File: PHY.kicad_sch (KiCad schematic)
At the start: 50 parts, among them U1 LAN83C185-JT, Y1 25 MHz

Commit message: Assign footprints to everything bar inductors
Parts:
- C5, C7: footprint (none) -> Capacitor_SMD:C_0805_2012Metric_Pad1.18x1.45mm_HandSolder
- D1, D2: footprint (none) -> LED_SMD:LED_1206_3216Metric_Pad1.42x1.75mm_HandSolder
- FB1, FB2, FB3: footprint (none) -> Inductor_SMD:L_1206_3216Metric_Pad1.22x1.90mm_HandSolder
- JP1, JP2, JP3, JP4: footprint (none) -> Jumper:SolderJumper-2_P1.3mm_Open_Pad1.0x1.5mm
- TP1: footprint (none) -> TestPoint:TestPoint_Pad_1.0x1.0mm
- Y1: footprint (none) -> Crystal:Crystal_SMD_Abracon_ABM3-2Pin_5.0x3.2mm_HandSoldering
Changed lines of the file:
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@@
       (effects (font (size 1.27 1.27)) (justify left))
     )
-    (property "Footprint" "" (id 2) (at 231.14 100.33 0)
+    (property "Footprint" "TestPoint:TestPoint_Pad_1.0x1.0mm" (id 2) (at 231.14 100.33 0)
       (effects (font (size 1.27 1.27)) hide)
     )
@@
     (property "Reference" "FB3" (id 0) (at 115.5192 165.1 90))
     (property "Value" "FerriteBead" (id 1) (at 115.5192 167.64 90))
-    (property "Footprint" "" (id 2) (at 115.57 174.498 90)
+    (property "Footprint" "Inductor_SMD:L_1206_3216Metric_Pad1.22x1.90mm_HandSolder" (id 2) (at 115.57 174.498 90)
       (effects (font (size 1.27 1.27)) hide)
     )
@@
       (effects (font (size 1.27 1.27)) (justify left))
     )
-    (property "Footprint" "" (id 2) (at 33.9852 129.54 0)
+    (property "Footprint" "Capacitor_SMD:C_0805_2012Metric_Pad1.18x1.45mm_HandSolder" (id 2) (at 33.9852 129.54 0)
       (effects (font (size 1.27 1.27)) hide)
     )
@@
     (property "Reference" "JP4" (id 0) (at 71.12 55.88 0))
     (property "Value" "SolderJumper_2_Open" (id 1) (at 71.12 58.42 0))
-    (property "Footprint" "" (id 2) (at 71.12 62.23 0)
+    (property "Footprint" "Jumper:SolderJumper-2_P1.3mm_Open_Pad1.0x1.5mm" (id 2) (at 71.12 62.23 0)
       (effects (font (size 1.27 1.27)) hide)
     )
@@
     (property "Reference" "JP2" (id 0) (at 71.12 50.8 0))
     (property "Value" "SolderJumper_2_Open" (id 1) (at 71.12 53.34 0))
-    (property "Footprint" "" (id 2) (at 71.12 57.15 0)
+    (property "Footprint" "Jumper:SolderJumper-2_P1.3mm_Open_Pad1.0x1.5mm" (id 2) (at 71.12 57.15 0)
       (effects (font (size 1.27 1.27)) hide)
     )
@@
     (property "Reference" "JP3" (id 0) (at 71.12 53.34 0))
     (property "Value" "SolderJumper_2_Open" (id 1) (at 71.12 55.88 0))
-    (property "Footprint" "" (id 2) (at 71.12 59.69 0)
+    (property "Footprint" "Jumper:SolderJumper-2_P1.3mm_Open_Pad1.0x1.5mm" (id 2) (at 71.12 59.69 0)
       (effects (font (size 1.27 1.27)) hide)
     )
@@
     (property "Reference" "FB1" (id 0) (at 27.8892 165.1 90))
     (property "Value" "FerriteBead" (id 1) (at 27.8892 167.64 90))
-    (property "Footprint" "" (id 2) (at 27.94 174.498 90)
+    (property "Footprint" "Inductor_SMD:L_1206_3216Metric_Pad1.22x1.90mm_HandSolder" (id 2) (at 27.94 174.498 90)
       (effects (font (size 1.27 1.27)) hide)
     )
@@
       (effects (font (size 1.27 1.27)) (justify right))
     )
-    (property "Footprint" "" (id 2) (at 269.24 33.02 0)
+    (property "Footprint" "LED_SMD:LED_1206_3216Metric_Pad1.42x1.75mm_HandSolder" (id 2) (at 269.24 33.02 0)
       (effects (font (size 1.27 1.27)) hide)
     )
@@
     (property "Reference" "FB2" (id 0) (at 79.9592 165.1 90))
     (property "Value" "FerriteBead" (id 1) (at 79.9592 167.64 90))
-    (property "Footprint" "" (id 2) (at 80.01 174.498 90)
+    (property "Footprint" "Inductor_SMD:L_1206_3216Metric_Pad1.22x1.90mm_HandSolder" (id 2) (at 80.01 174.498 90)
       (effects (font (size 1.27 1.27)) hide)
     )
@@
     (property "Reference" "Y1" (id 0) (at 27.94 111.76 0))
     (property "Value" "25 MHz" (id 1) (at 27.94 114.3 0))
-    (property "Footprint" "" (id 2) (at 27.94 119.38 0)
+    (property "Footprint" "Crystal:Crystal_SMD_Abracon_ABM3-2Pin_5.0x3.2mm_HandSoldering" (id 2) (at 27.94 119.38 0)
       (effects (font (size 1.27 1.27)) hide)
     )
@@
     (property "Reference" "JP1" (id 0) (at 71.12 45.72 0))
     (property "Value" "SolderJumper_2_Open" (id 1) (at 71.12 48.26 0))
-    (property "Footprint" "" (id 2) (at 71.12 52.07 0)
+    (property "Footprint" "Jumper:SolderJumper-2_P1.3mm_Open_Pad1.0x1.5mm" (id 2) (at 71.12 52.07 0)
       (effects (font (size 1.27 1.27)) hide)
     )
@@
       (effects (font (size 1.27 1.27)) (justify right))
     )
-    (property "Footprint" "" (id 2) (at 219.71 31.75 0)
+    (property "Footprint" "LED_SMD:LED_1206_3216Metric_Pad1.42x1.75mm_HandSolder" (id 2) (at 219.71 31.75 0)
       (effects (font (size 1.27 1.27)) hide)
     )
@@
       (effects (font (size 1.27 1.27)) (justify left))
     )
-    (property "Footprint" "" (id 2) (at 23.8252 129.54 0)
-      (effects (font (size 1.27 1.27)) hide)
-    )
+    (property "Footprint" "Capacitor_SMD:C_0805_2012Metric_Pad1.18x1.45mm_HandSolder" (id 2) (at 23.8252 129.54 0)
+      (effects (font (size 1.27 1.27)) hide)
+    )

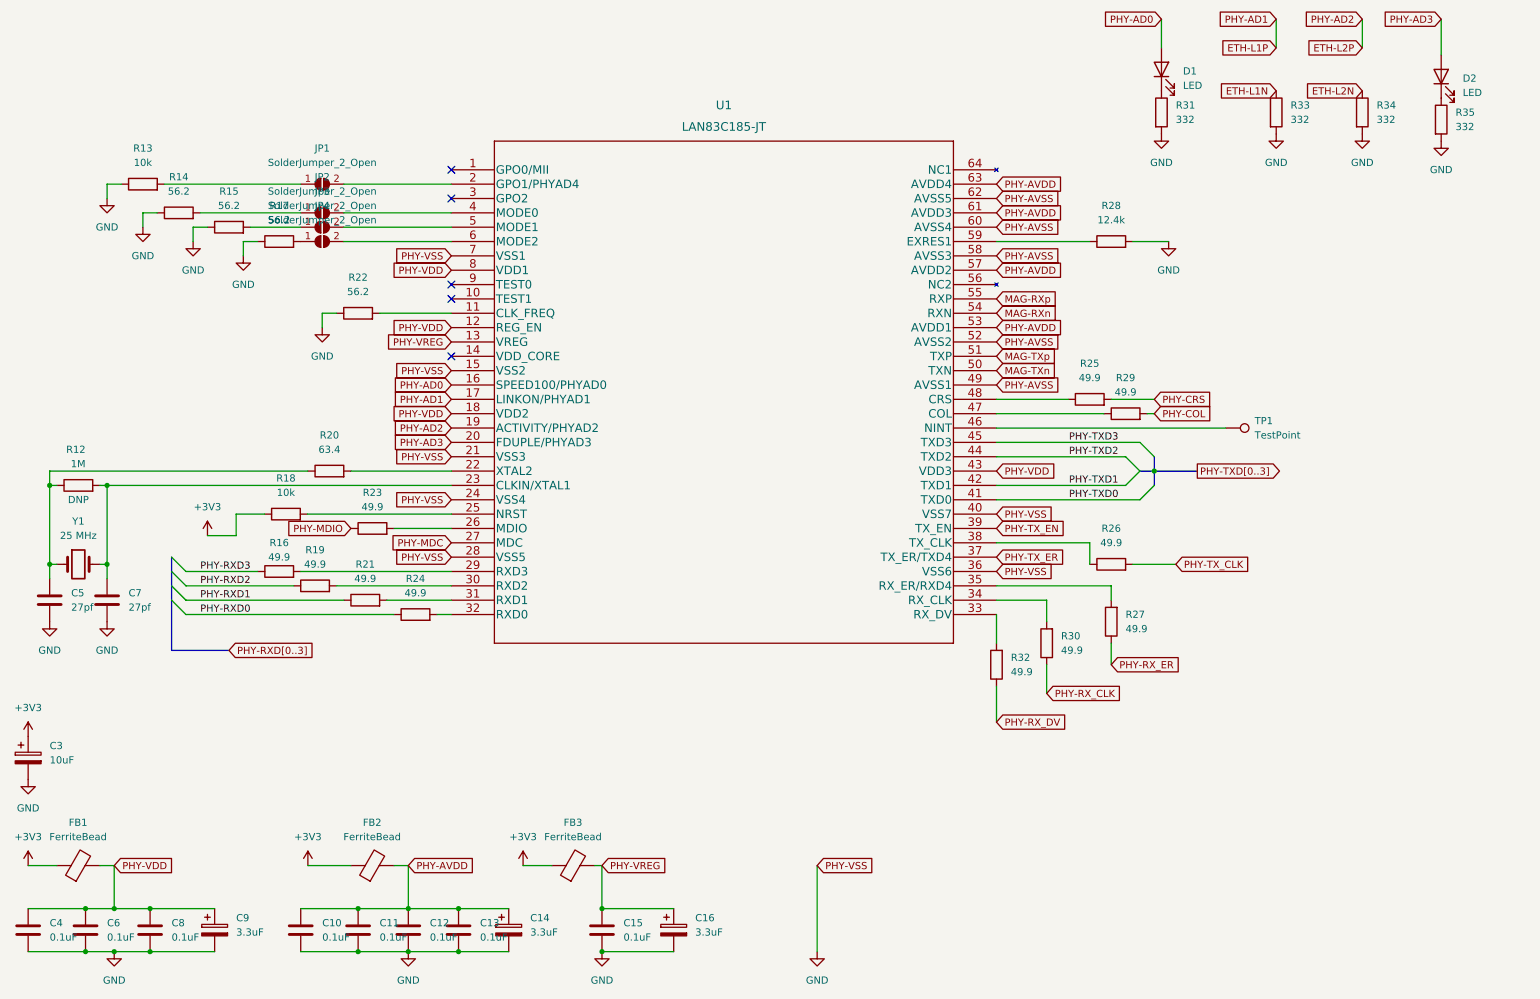
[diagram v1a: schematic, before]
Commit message: added most of the sourcing info
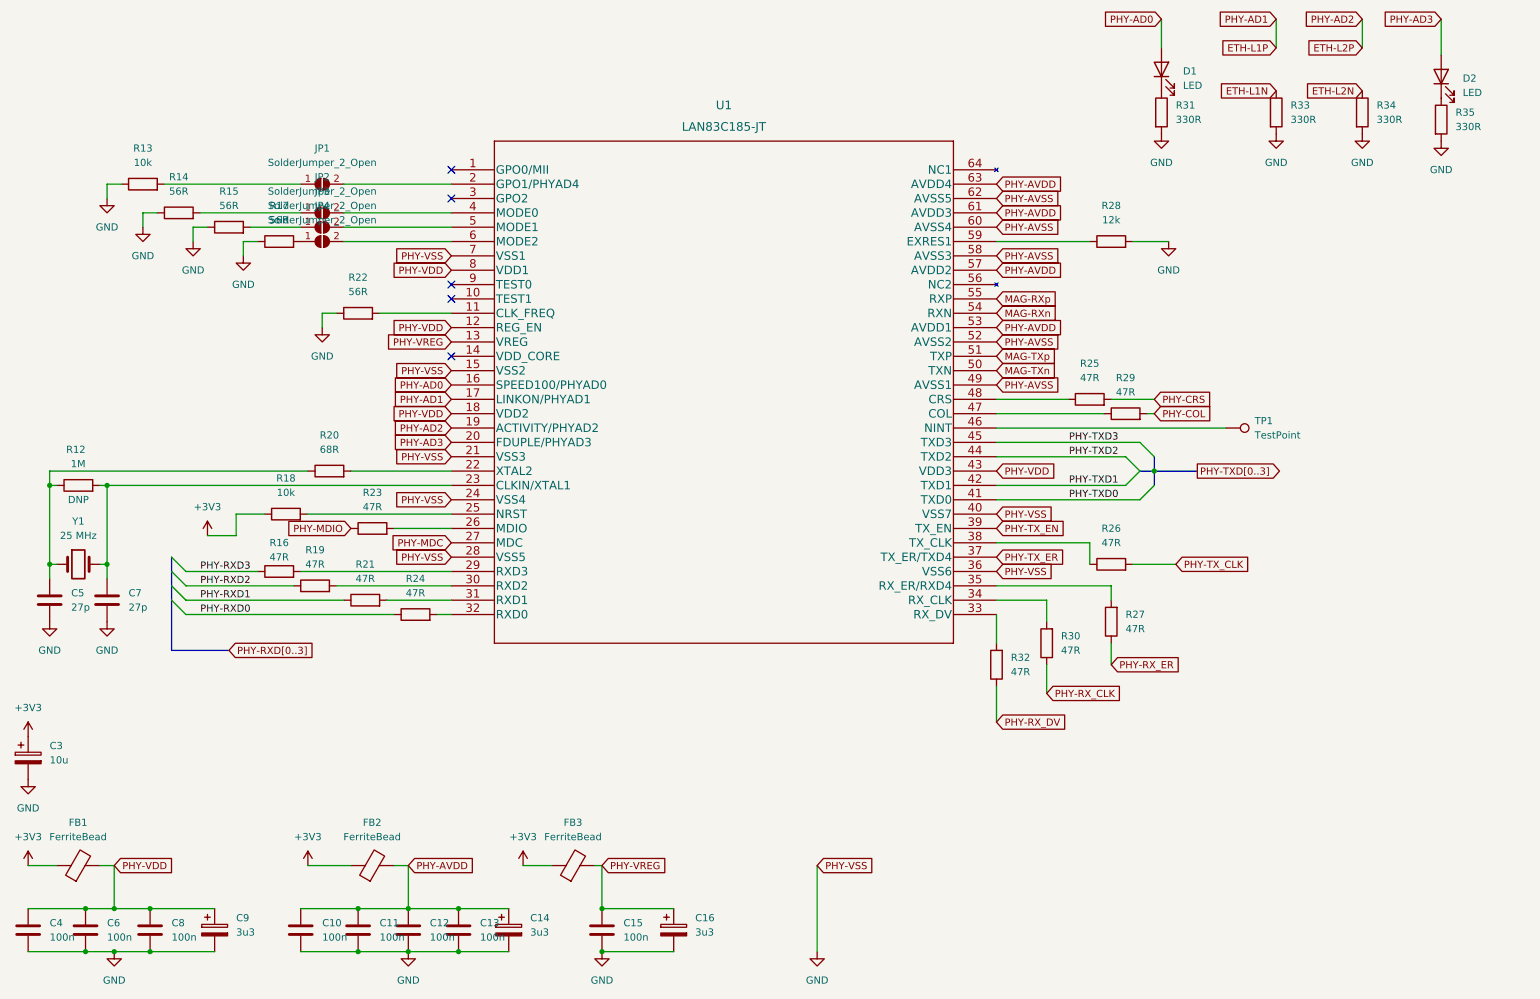
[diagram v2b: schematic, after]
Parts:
- C10, C11, C12, C13, C15, C4, C6, C8: value 0.1uF -> 100n; Source (none) -> L3 store
- C14, C16, C9: value 3.3uF -> 3u3; Source (none) -> L3 store
- C3: value 10uF -> 10u; Source (none) -> L3 store
- C5, C7: value 27pf -> 27p; Source (none) -> https://onecall.farnell.com/multicomp/mc0805n270j500ct/cap-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
- D1: Source (none) -> https://onecall.farnell.com/dialight/599-0240-007f/led-yell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
- D2: Source (none) -> https://onecall.farnell.com/dialight/599-0281-007f/led-gree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
- FB1, FB2, FB3: Source (none) -> https://uk.farnell.com/bourns/mh3261-601y/ferrite-bead-0-1o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
- JP1, JP2, JP3, JP4, TP1: Source (none) -> pcb
- R12, R13, R18: Source (none) -> L3 store
- R14, R15, R17, R22: value 56.2 -> 56R; Source (none) -> L3 store
- R16, R19, R21, R23, R24, R25, R26, R27, R29, R30, R32: value 49.9 -> 47R; Source (none) -> L3 store
- R20: value 63.4 -> 68R; Source (none) -> L3 store
- R28: value 12.4k -> 12k; Source (none) -> L3 store
- R31, R33, R34, R35: value 332 -> 330R; Source (none) -> L3 store
- U1: Source (none) -> https://uk.rs-online.com/web/p/physical-layer-transceivers/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
- Y1: Source (none) -> https://onecall.farnell.com/abracon/abm3-25-000mhz-d2y-t/cr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

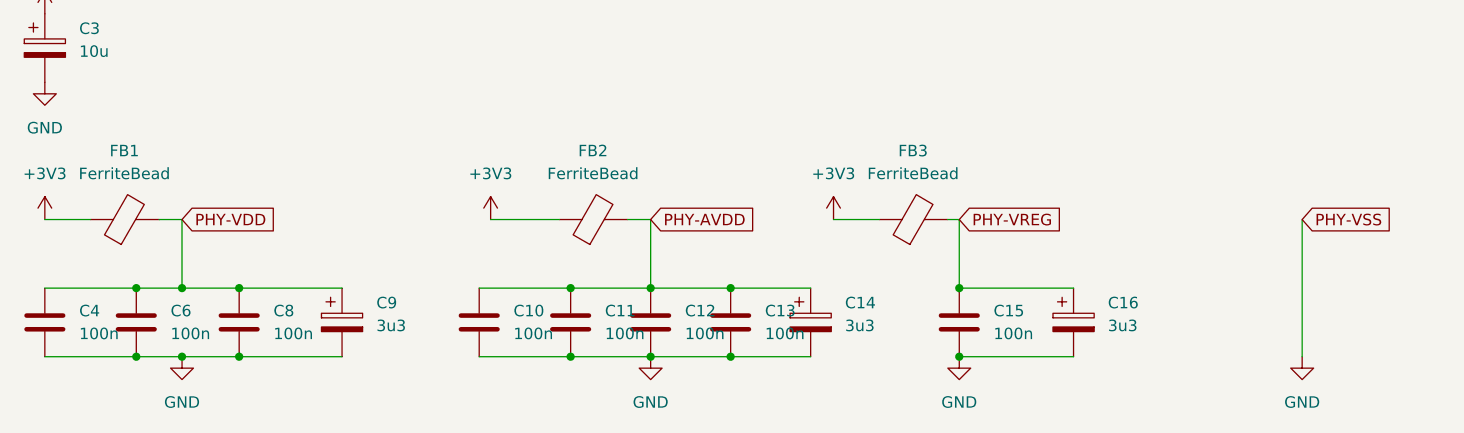
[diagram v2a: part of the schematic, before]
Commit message: solved power drc problems
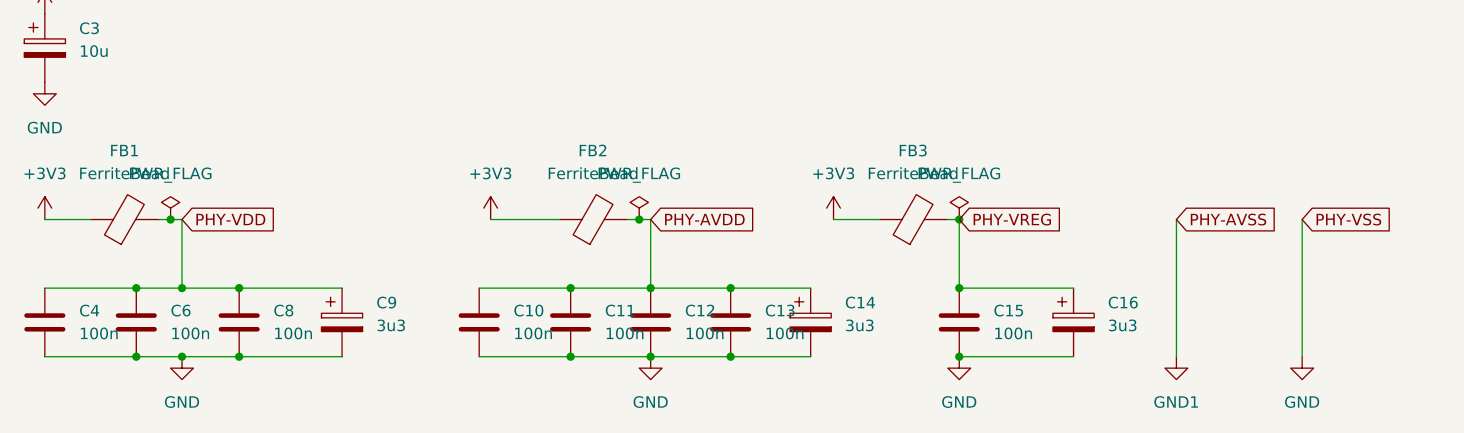
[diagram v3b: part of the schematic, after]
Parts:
- U1: Source https://uk.rs-online.com/web/p/physical-layer-transceivers/9101828 -> https://uk.rs-online.com/web/p/physical-layer-transceivers/6726806
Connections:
- net PHY-AVSS renamed GND1
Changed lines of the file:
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@@
   (junction (at 120.65 187.96) (diameter 0) (color 0 0 0 0)
   )
+  (junction (at 85.09 172.72) (diameter 0) (color 0 0 0 0)
+  )
+  (junction (at 120.65 172.72) (diameter 0) (color 0 0 0 0)
+  )
   (junction (at 34.29 180.34) (diameter 0) (color 0 0 0 0)
   )
@@
   )
   (junction (at 33.02 119.38) (diameter 0) (color 0 0 0 0)
+  )
+  (junction (at 33.02 172.72) (diameter 0) (color 0 0 0 0)
   )
   (junction (at 29.21 180.34) (diameter 0) (color 0 0 0 0)
@@
     (stroke (width 0) (type default) (color 0 0 0 0))
   )
+  (wire (pts (xy 144.78 172.72) (xy 144.78 187.96))
+    (stroke (width 0) (type default) (color 0 0 0 0))
+  )
   (wire (pts (xy 71.12 74.93) (xy 71.12 77.47))
     (stroke (width 0) (type default) (color 0 0 0 0))
@@
     (stroke (width 0) (type default) (color 0 0 0 0))
   )
-  (wire (pts (xy 31.75 172.72) (xy 34.29 172.72))
+  (wire (pts (xy 31.75 172.72) (xy 33.02 172.72))
     (stroke (width 0) (type default) (color 0 0 0 0))
   )
@@
     (stroke (width 0) (type default) (color 0 0 0 0))
   )
+  (wire (pts (xy 85.09 172.72) (xy 86.36 172.72))
+    (stroke (width 0) (type default) (color 0 0 0 0))
+  )
   (wire (pts (xy 255.27 22.86) (xy 255.27 27.94))
     (stroke (width 0) (type default) (color 0 0 0 0))
@@
     (stroke (width 0) (type default) (color 0 0 0 0))
   )
+  (wire (pts (xy 33.02 172.72) (xy 34.29 172.72))
+    (stroke (width 0) (type default) (color 0 0 0 0))
+  )
   (wire (pts (xy 46.99 128.27) (xy 83.82 128.27))
     (stroke (width 0) (type default) (color 0 0 0 0))
@@
     (stroke (width 0) (type default) (color 0 0 0 0))
   )
-  (wire (pts (xy 83.82 172.72) (xy 86.36 172.72))
+  (wire (pts (xy 83.82 172.72) (xy 85.09 172.72))
     (stroke (width 0) (type default) (color 0 0 0 0))
   )
@@
     )
   )
+  (global_label "PHY-AVSS" (shape input) (at 144.78 172.72 0) (fields_autoplaced)
+    (effects (font (size 1.27 1.27)) (justify left))
+    (property "Intersheet References" "${INTERSHEET_REFS}" (id 0) (at 157.0507 172.6406 0)
+      (effects (font (size 1.27 1.27)) (justify left) hide)
+    )
+  )
   (global_label "PHY-AVDD" (shape input) (at 190.5 67.31 0) (fields_autoplaced)
     (effects (font (size 1.27 1.27)) (justify left))
@@
       (effects (font (size 1.27 1.27)) (justify right) hide)
     )
+  )
+  (symbol (lib_id "power:PWR_FLAG") (at 85.09 172.72 0) (unit 1)
+    (in_bom yes) (on_board yes) (fields_autoplaced)
+    (property "Reference" "#FLG0106" (id 0) (at 85.09 170.815 0)
+      (effects (font (size 1.27 1.27)) hide)
+    )
+    (property "Value" "PWR_FLAG" (id 1) (at 85.09 167.64 0))
+    (property "Footprint" "" (id 2) (at 85.09 172.72 0)
+      (effects (font (size 1.27 1.27)) hide)
+    )
+    (property "Datasheet" "~" (id 3) (at 85.09 172.72 0)
+      (effects (font (size 1.27 1.27)) hide)
+    )
+    (pin "1")
   )
   (symbol (lib_id "Device:R") (at 207.01 90.17 90) (unit 1)
@@
     (pin "2")
   )
+  (symbol (lib_id "power:PWR_FLAG") (at 33.02 172.72 0) (unit 1)
+    (in_bom yes) (on_board yes) (fields_autoplaced)
+    (property "Reference" "#FLG0105" (id 0) (at 33.02 170.815 0)
+      (effects (font (size 1.27 1.27)) hide)
+    )
+    (property "Value" "PWR_FLAG" (id 1) (at 33.02 167.64 0))
+    (property "Footprint" "" (id 2) (at 33.02 172.72 0)
+      (effects (font (size 1.27 1.27)) hide)
+    )
+    (property "Datasheet" "~" (id 3) (at 33.02 172.72 0)
+      (effects (font (size 1.27 1.27)) hide)
+    )
+    (pin "1")
+  )
   (symbol (lib_id "Device:FerriteBead") (at 115.57 172.72 90) (unit 1)
     (in_bom yes) (on_board yes) (fields_autoplaced)
@@
     (pin "2")
   )
+  (symbol (lib_id "power:PWR_FLAG") (at 120.65 172.72 0) (unit 1)
+    (in_bom yes) (on_board yes) (fields_autoplaced)
+    (property "Reference" "#FLG0104" (id 0) (at 120.65 170.815 0)
+      (effects (font (size 1.27 1.27)) hide)
+    )
+    (property "Value" "PWR_FLAG" (id 1) (at 120.65 167.64 0))
+    (property "Footprint" "" (id 2) (at 120.65 172.72 0)
+      (effects (font (size 1.27 1.27)) hide)
+    )
+    (property "Datasheet" "~" (id 3) (at 120.65 172.72 0)
+      (effects (font (size 1.27 1.27)) hide)
+    )
+    (pin "1")
+  )
   (symbol (lib_id "Device:R") (at 255.27 39.37 0) (unit 1)
     (in_bom yes) (on_board yes) (fields_autoplaced)
@@
     (pin "1")
     (pin "2")
+  )
+  (symbol (lib_id "power:GND1") (at 144.78 187.96 0) (unit 1)
+    (in_bom yes) (on_board yes) (fields_autoplaced)
+    (property "Reference" "#PWR0110" (id 0) (at 144.78 194.31 0)
+      (effects (font (size 1.27 1.27)) hide)
+    )
+    (property "Value" "GND1" (id 1) (at 144.78 193.04 0))
+    (property "Footprint" "" (id 2) (at 144.78 187.96 0)
+      (effects (font (size 1.27 1.27)) hide)
+    )
+    (property "Datasheet" "" (id 3) (at 144.78 187.96 0)
+      (effects (font (size 1.27 1.27)) hide)
+    )
+    (pin "1")
   )
   (symbol (lib_id "Device:R") (at 210.82 129.54 180) (unit 1)
@@
       (effects (font (size 1.524 1.524)) hide)
     )
-    (property "Datasheet" "" (id 3) (at 93.98 49.53 0)
-      (effects (font (size 1.524 1.524)))
-    )
-    (property "Source" "https://uk.rs-online.com/web/p/physical-layer-transceivers/9101828" (id 4) (at 93.98 49.53 0)
-      (effects (font (size 1.27 1.27)) hide)
-    )
+    (property "Datasheet" "https://docs.rs-online.com/1038/0900766b80d9640a.pdf" (id 3) (at 93.98 49.53 0)
+      (effects (font (size 1.524 1.524)) hide)
+    )
+    (property "Source" "https://uk.rs-online.com/web/p/physical-layer-transceivers/6726806" (id 4) (at 93.98 49.53 0)
+      (effects (font (size 1.27 1.27)) hide)
+    )

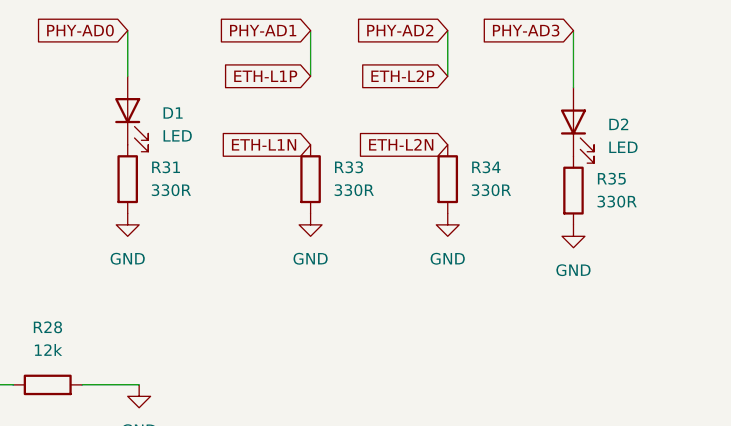
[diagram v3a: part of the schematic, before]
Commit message: Add SMA connector footprint and assign source
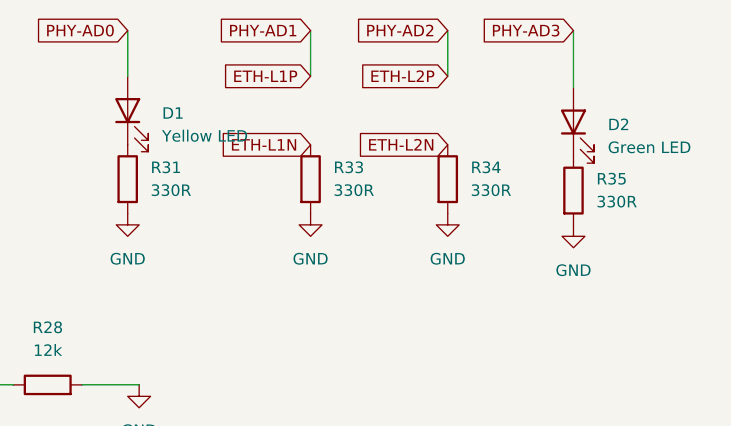
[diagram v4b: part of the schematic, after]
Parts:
- D1: value LED -> Yellow LED
- D2: value LED -> Green LED
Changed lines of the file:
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@@
       (effects (font (size 1.27 1.27)) (justify right))
     )
-    (property "Value" "LED" (id 1) (at 273.05 35.8774 90)
+    (property "Value" "Green LED" (id 1) (at 273.05 35.8774 90)
       (effects (font (size 1.27 1.27)) (justify right))
     )
@@
       (effects (font (size 1.27 1.27)) (justify right))
     )
-    (property "Value" "LED" (id 1) (at 223.52 34.6074 90)
-      (effects (font (size 1.27 1.27)) (justify right))
-    )
+    (property "Value" "Yellow LED" (id 1) (at 223.52 34.6074 90)
+      (effects (font (size 1.27 1.27)) (justify right))
+    )
